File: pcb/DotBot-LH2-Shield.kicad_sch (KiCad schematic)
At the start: 23 parts, among them J1 Conn_01x04, J1 Conn_01x10, Q1 NX6008NBKWX, Q2 NX6008NBKWX, Q3 NX6008NBKWX, U3 ISM330DHCXTR, U4 LIS3MDL, U4 TS4231

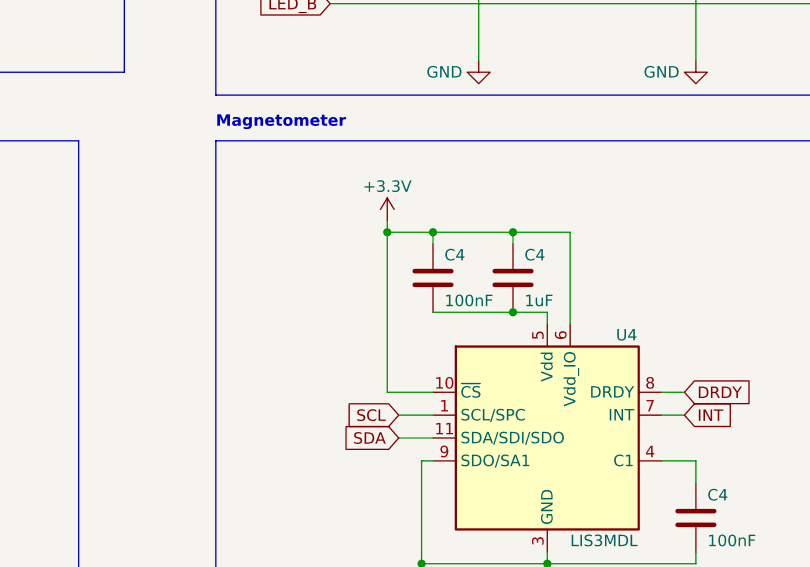
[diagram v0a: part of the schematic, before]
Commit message: LH2 shield: fix LIS3MDL setup
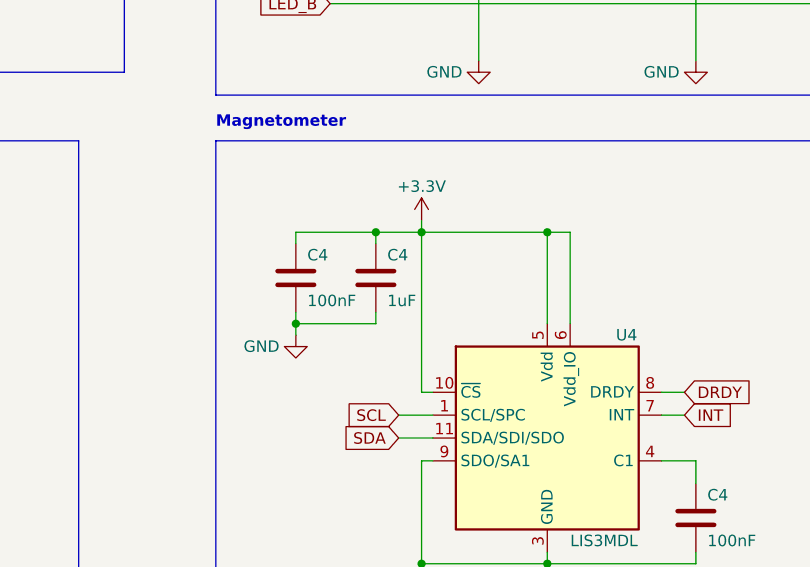
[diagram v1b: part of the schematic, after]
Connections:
- net +3V3: now also U4.5 (Vdd)
- net GND: now also C4.2, C4.2
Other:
- moved on the sheet: C4
